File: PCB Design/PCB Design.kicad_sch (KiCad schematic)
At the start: 17 parts, among them J1 Conn_01x02_Pin, Q1 2N2222, Q2 2N2907, Q3 2N2222, Q4 2N2907, U1 INA219AxD

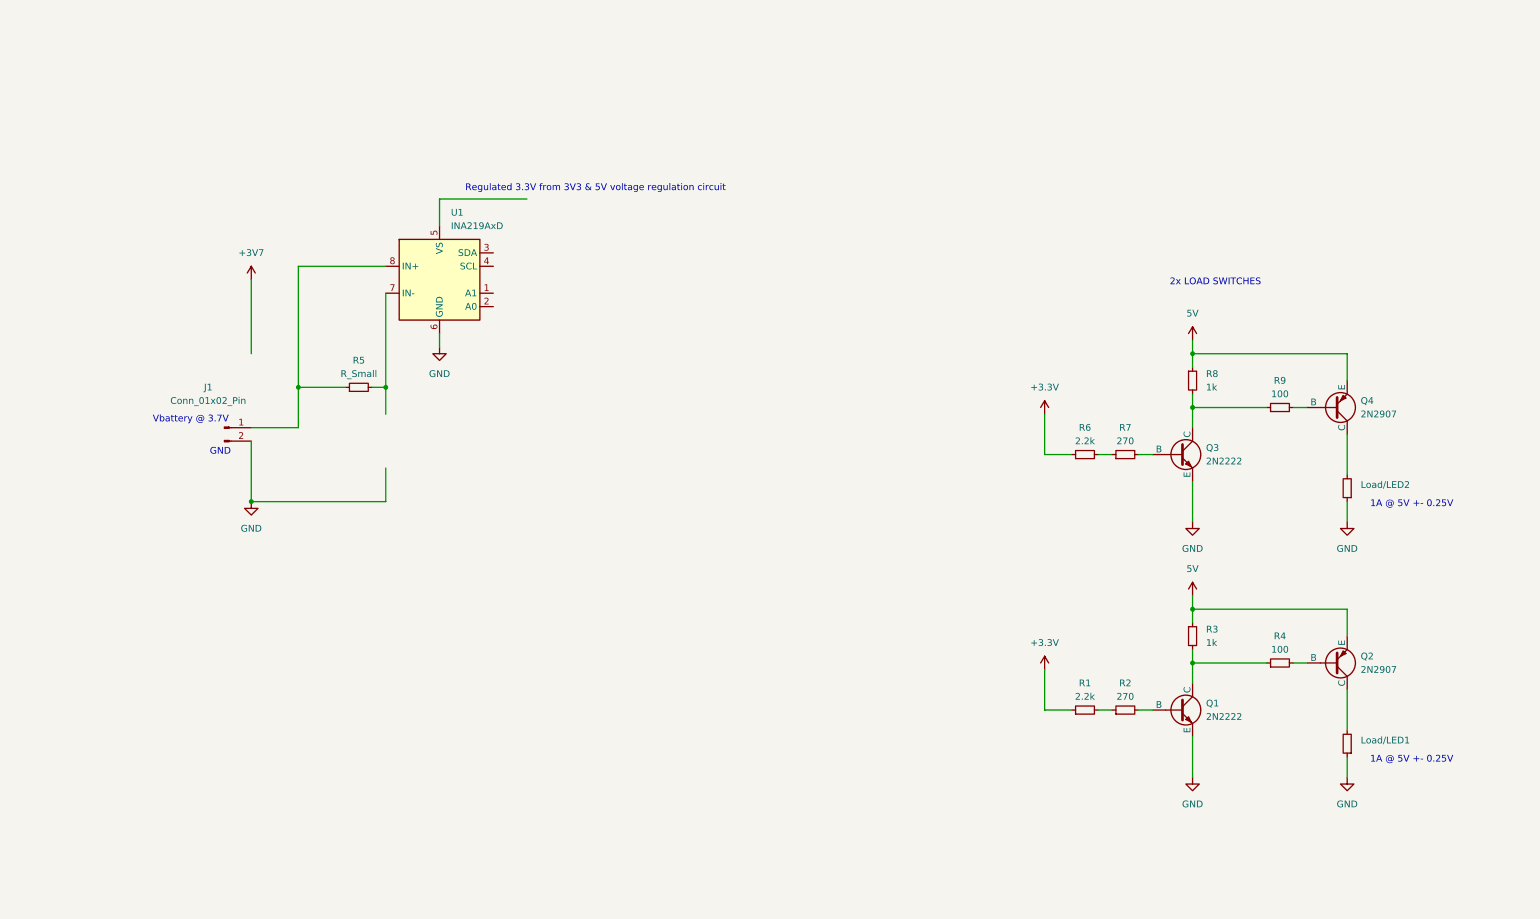
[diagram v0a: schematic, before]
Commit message: Added USB-C trigger IC to get 9V instead of standard 5V
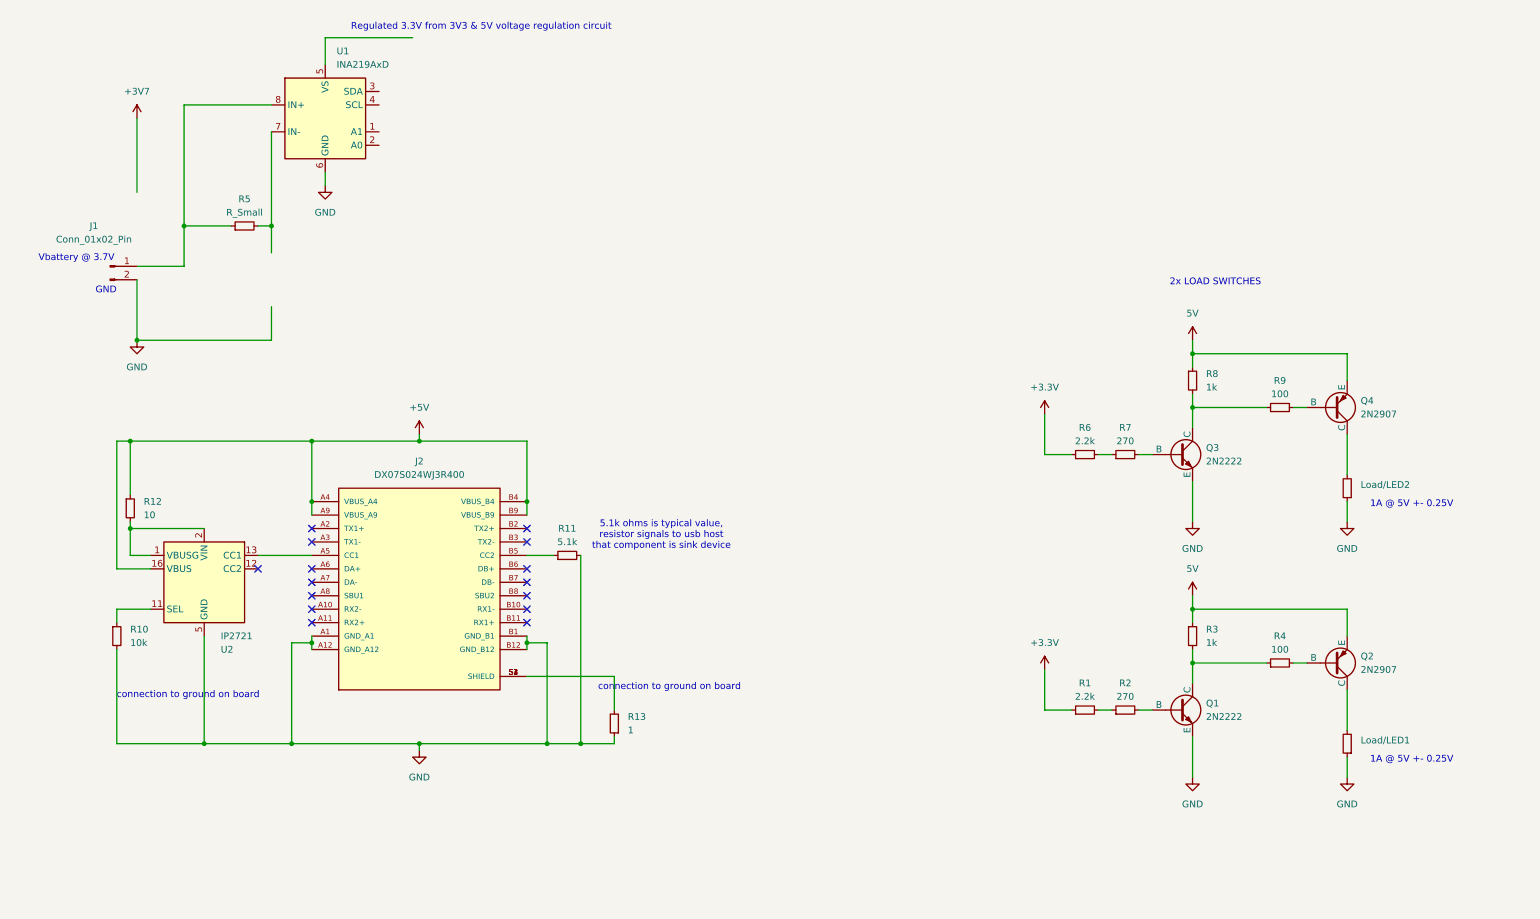
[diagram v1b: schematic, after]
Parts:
- added J2: DX07S024WJ3R400, DX07S024WJ3R400:JAE_DX07S024WJ3R400, symbol DX07S024WJ3R400:DX07S024WJ3R400
- added R10: 10k, symbol Device:R_Small
- added R11: 5.1k, symbol Device:R_Small
- added R12: 10, symbol Device:R_Small
- added R13: 1, symbol Device:R_Small
- added U2: IP2721, Package_SO:TSSOP-16_4.4x5mm_P0.65mm, symbol Interface_USB:IP2721
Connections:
- net GND: now also J2.A1 (GND_A1), J2.A12 (GND_A12), J2.B1 (GND_B1), J2.B12 (GND_B12), R10.2, R11.2, R13.1, U2.5 (GND)
- new net: J2.S1 (SHIELD), J2.S2 (SHIELD), J2.S3 (SHIELD), J2.S4 (SHIELD), R13.2
- new net: J2.A5 (CC1), U2.13 (CC1)
- new net: J2.B5 (CC2), R11.1
- new net: R12.2, U2.1 (VBUSG), U2.2 (VIN)
- new net: R10.1, U2.11 (SEL)
- new net +5V: J2.A4 (VBUS_A4), J2.A9 (VBUS_A9), J2.B4 (VBUS_B4), J2.B9 (VBUS_B9), R12.1, U2.16 (VBUS)
- no-connect marks 0 -> 15
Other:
- note added: "5.1k ohms is typical value, resistor signals to usb host that component is sink device"
- note added: "connection to ground on board"
- moved on the sheet: J1, R5, U1

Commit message: Added 32 pin connector and some net labels.
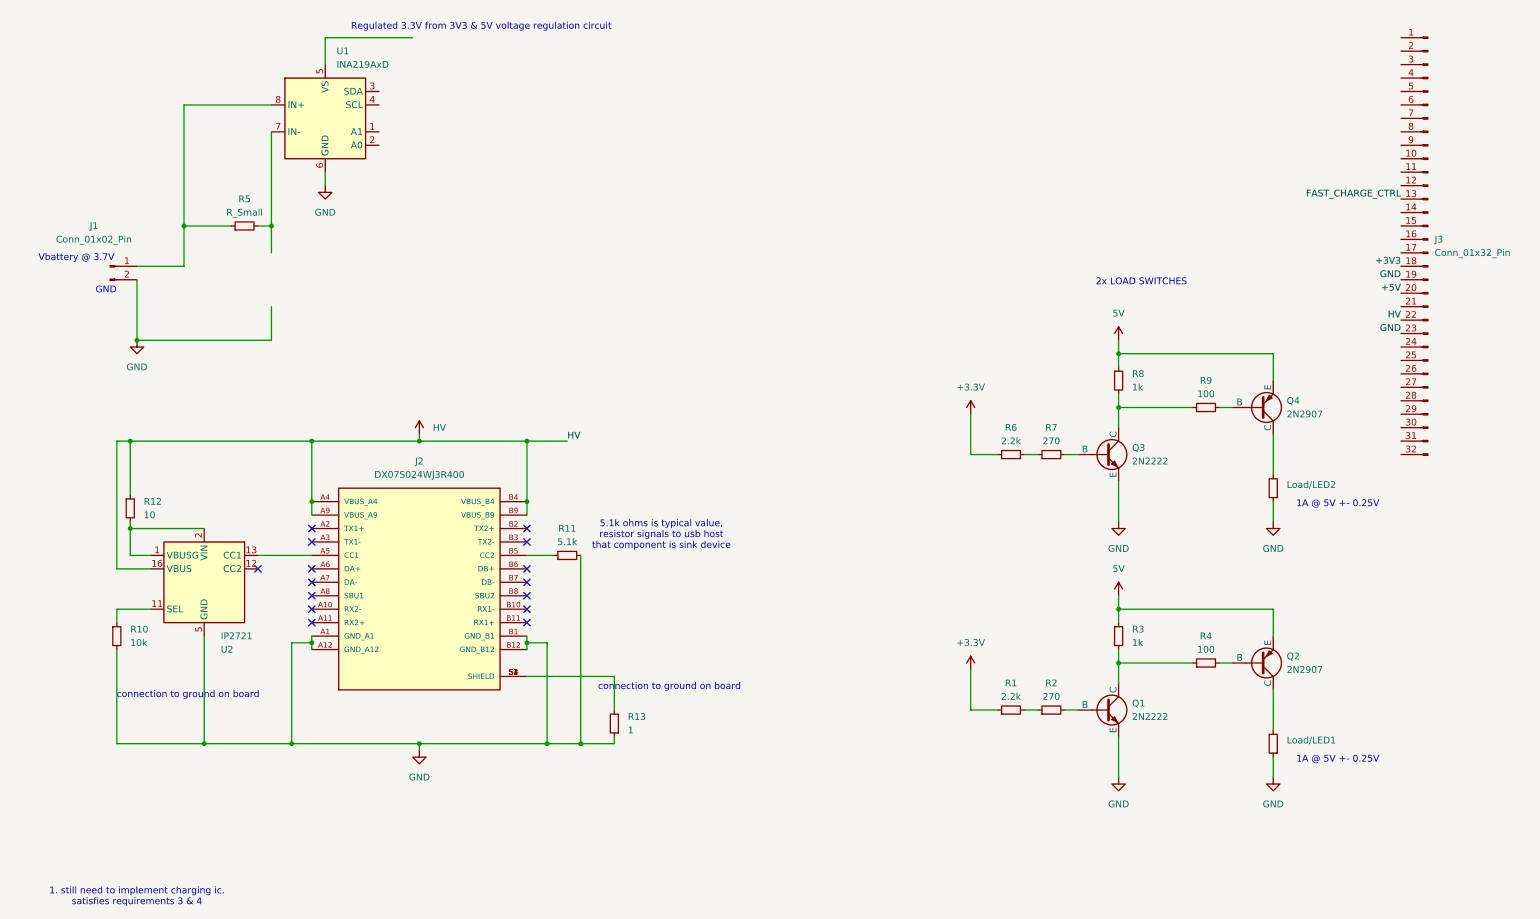
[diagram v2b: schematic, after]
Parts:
- added J3: Conn_01x32_Pin, symbol Connector:Conn_01x32_Pin
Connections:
- net +5V: now also J3.20 (Pin_20); no longer J2.A4 (VBUS_A4), J2.A9 (VBUS_A9), J2.B4 (VBUS_B4), J2.B9 (VBUS_B9), R12.1, U2.16 (VBUS)
- net GND: now also J3.19 (Pin_19), J3.23 (Pin_23)
- new net +3V3: J3.18 (Pin_18)
- new net FAST_CHARGE_CTRL: J3.13 (Pin_13)
- new net HV: J2.A4 (VBUS_A4), J2.A9 (VBUS_A9), J2.B4 (VBUS_B4), J2.B9 (VBUS_B9), J3.22 (Pin_22), R12.1, U2.16 (VBUS)
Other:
- note added: "1. still need to implement charging ic. satisfies requirements 3 & 4"
- moved on the sheet: Load/LED1, Load/LED2, Q1, Q2, Q3, Q4, R1, R2, R3, R4, R6, R7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

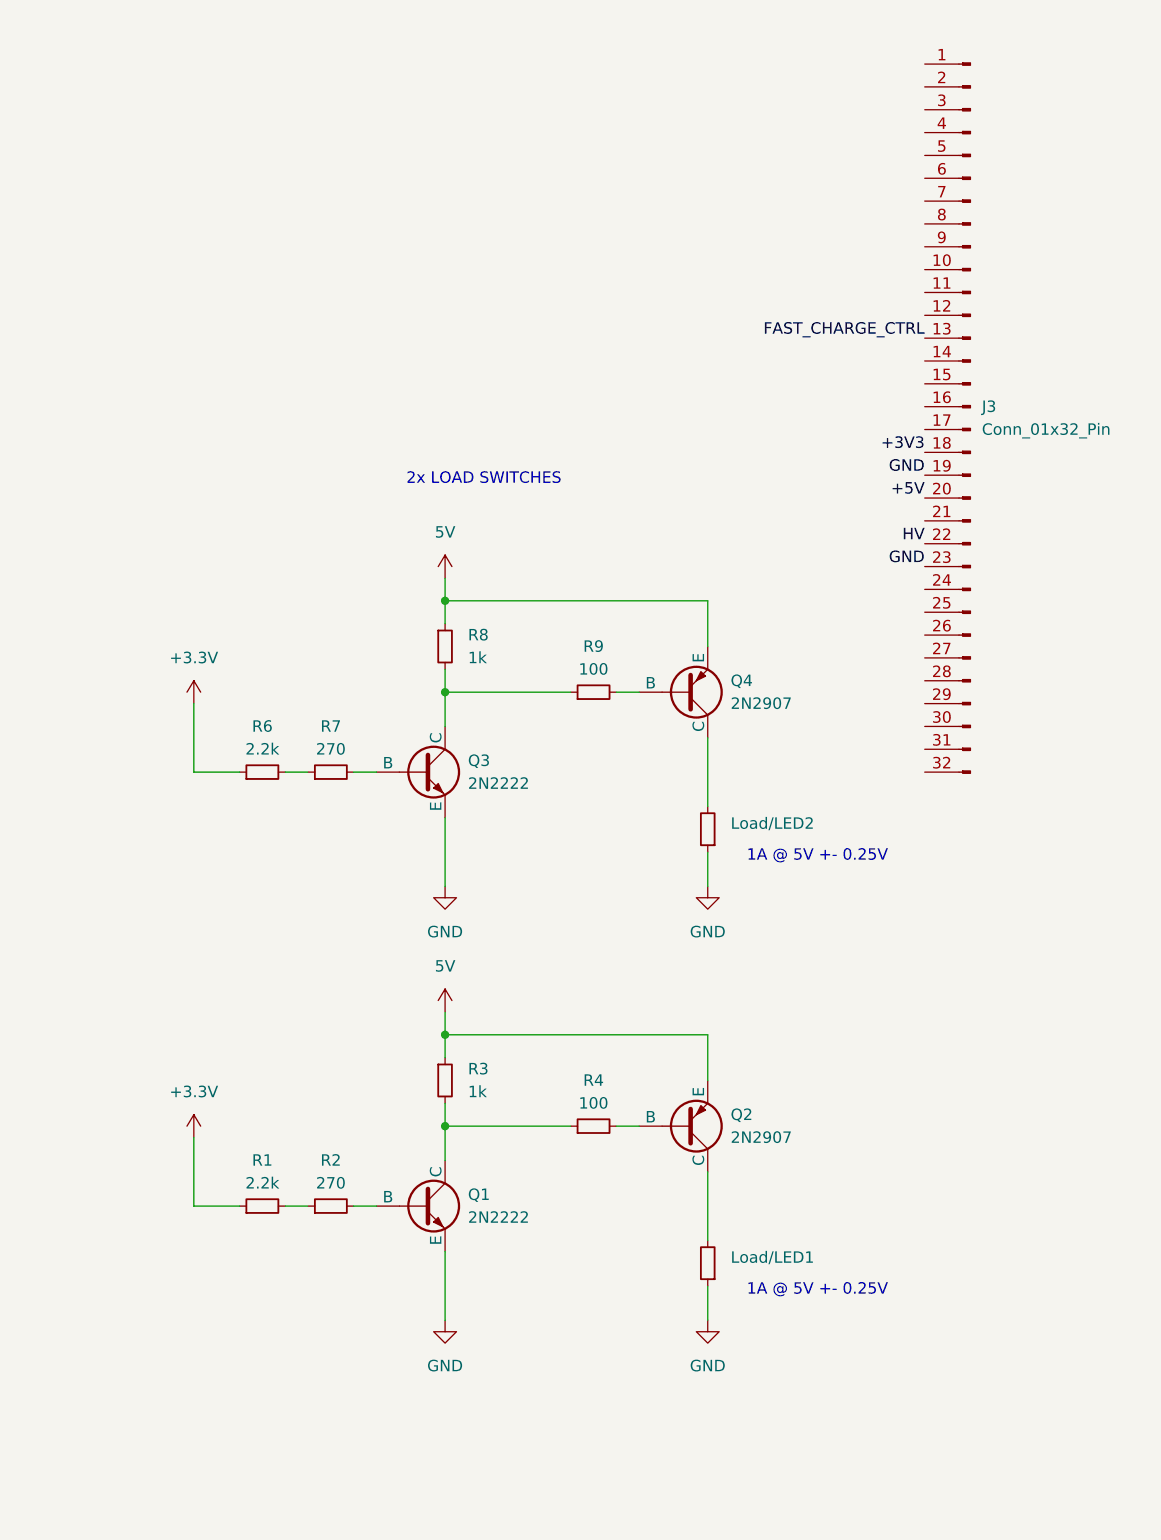
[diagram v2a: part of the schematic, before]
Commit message: Replaced 32 pin connector with 2x16 pin connector. Replaced 2 load switch circuits with 2 load swicth ICs.
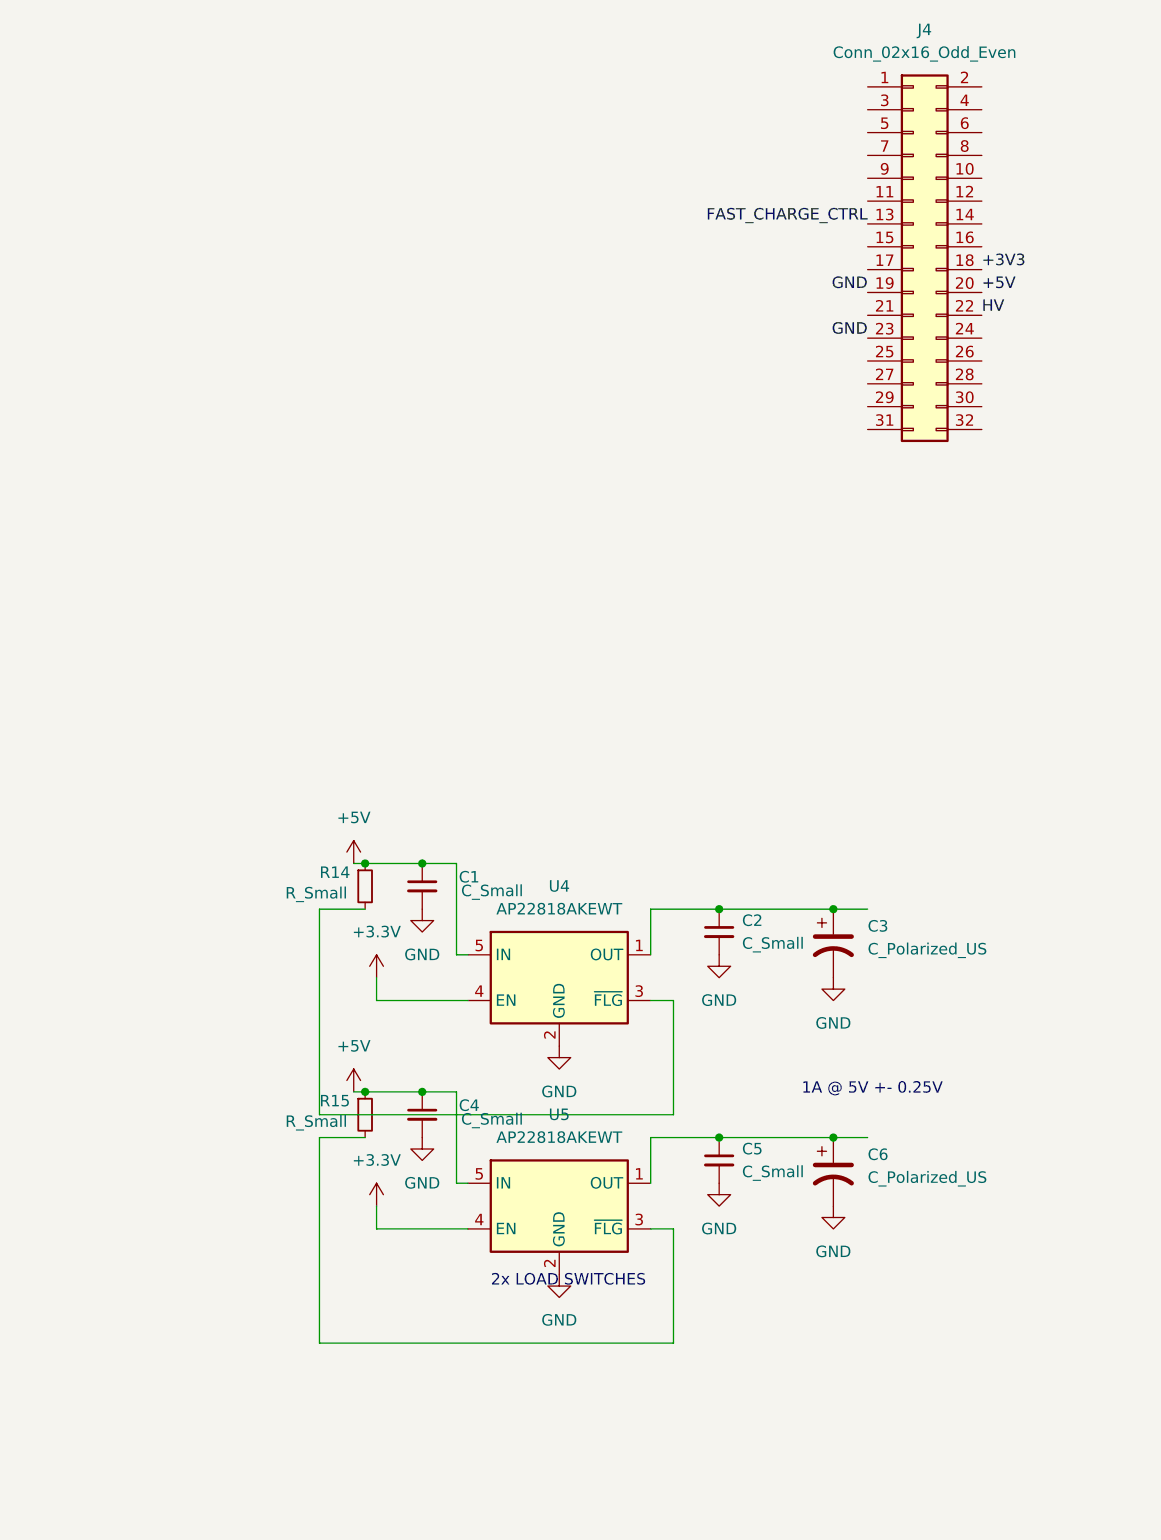
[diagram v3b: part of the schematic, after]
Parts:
- removed J3: Conn_01x32_Pin, symbol Connector:Conn_01x32_Pin
- removed Load/LED1, Load/LED2: ~, symbol Device:R_Small
- removed Q1, Q3: 2N2222, symbol Simulation_SPICE:NPN
- removed Q2, Q4: 2N2907, symbol Simulation_SPICE:PNP
- removed R1, R6: 2.2k, symbol Device:R_Small
- removed R2, R7: 270, symbol Device:R_Small
- removed R3, R8: 1k, symbol Device:R_Small
- removed R4, R9: 100, symbol Device:R_Small
- added C1, C2, C4, C5: C_Small, symbol Device:C_Small
- added C3, C6: C_Polarized_US, symbol Device:C_Polarized_US
- added J4: Conn_02x16_Odd_Even, symbol Connector_Generic:Conn_02x16_Odd_Even
- added R14, R15: R_Small, symbol Device:R_Small
- added U4, U5: AP22818AKEWT, Package_TO_SOT_SMD:SOT-23-5, symbol Power_Management:AP22818AKEWT
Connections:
- net +3.3V: now also U4.4 (EN), U5.4 (EN)
- net +3V3: now also J4.18 (Pin_18)
- net +5V: now also C1.1, C4.1, J4.20 (Pin_20), R14.1, R15.1, U4.5 (IN), U5.5 (IN)
- net FAST_CHARGE_CTRL: now also J4.13 (Pin_13)
- net GND: now also C1.2, C2.2, C3.2, C4.2, C5.2, C6.2, J4.19 (Pin_19), J4.23 (Pin_23), U4.2 (GND), U5.2 (GND)
- net HV: now also J4.22 (Pin_22)
- new net: C5.1, C6.1, U5.1 (OUT)
- new net: C2.1, C3.1, U4.1 (OUT)
- new net: R14.2, U4.3 (~{FLG})
- new net: R15.2, U5.3 (~{FLG})
